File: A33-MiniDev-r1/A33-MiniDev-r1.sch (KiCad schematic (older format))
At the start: 79 parts, among them IC1 AXP223, IC2 IS43TR16640CL-125JBLI, Q1 CSD25310Q2T, U1 A33, U2 A33

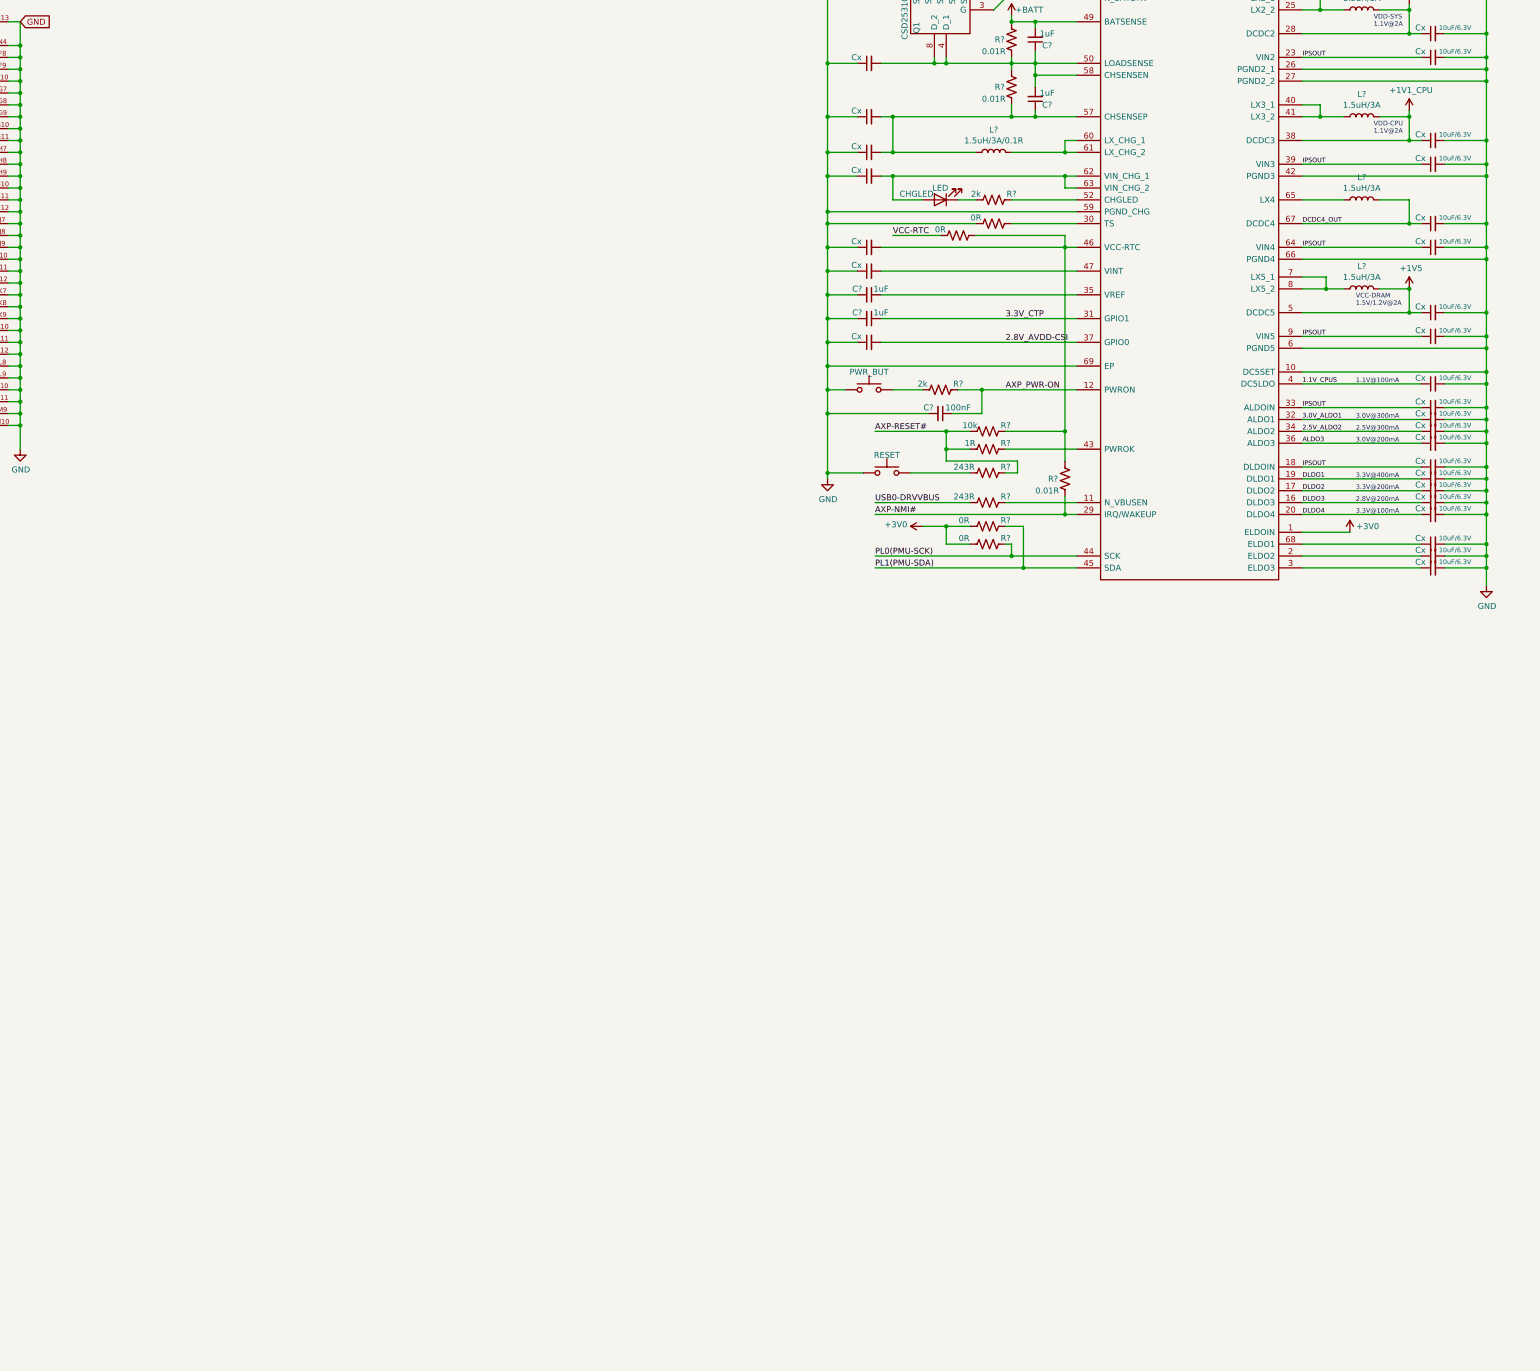
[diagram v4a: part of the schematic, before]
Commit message: Major library rework; added SD Card and WiFi module components
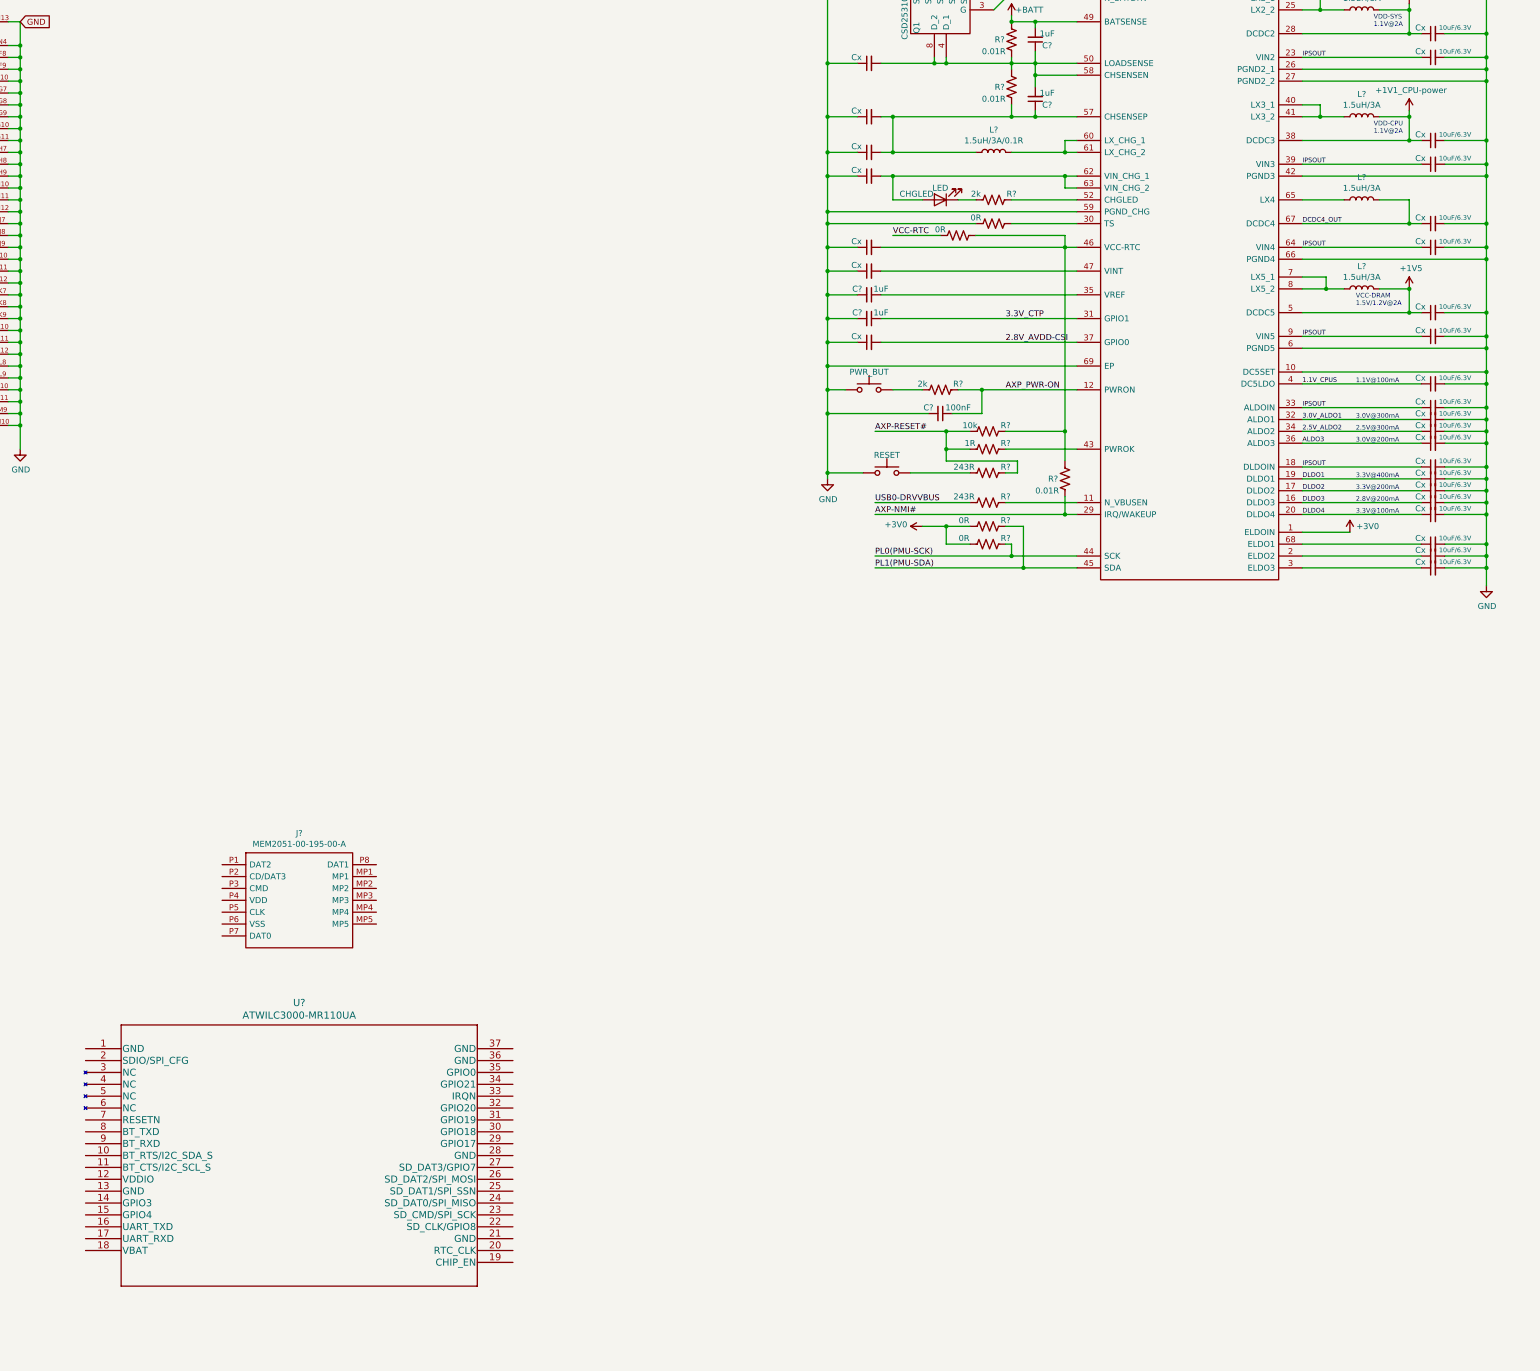
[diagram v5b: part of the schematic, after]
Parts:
- added J?: MEM2051-00-195-00-A, MEM20510019500A, symbol MEM2051-00-195-00-A:MEM2051-00-195-00-A
- added U?: ATWILC3000-MR110UA, ATWILC3000-MR110_MCH, symbol ATWILC3000-MR110UA:ATWILC3000-MR110UA
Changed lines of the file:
@@
 $EndComp
 $Comp
-L power:+1V1_CPU #PWR?
+L A33-MiniDev:+1V1_CPU-power #PWR?
 U 1 1 61CA9E70
 P 18300 3250
 F 0 "#PWR?" H 18300 3100 50  0001 C CNN
-F 1 "+1V1_CPU" H 18315 3423 50  0000 C CNN
+F 1 "+1V1_CPU-power" H 18315 3423 50  0000 C CNN
 F 2 "" H 18300 3250 50  0001 C CNN
 F 3 "" H 18300 3250 50  0001 C CNN
@@
 Wire Wire Line
 	20600 1150 20600 1250
+Connection ~ 20600 1250
 Wire Bus Line
 	3500 3300 3500 3500
@@
 Wire Bus Line
 	3700 11400 3700 14500
-Connection ~ 20600 1250
+$Comp
+L MEM2051-00-195-00-A:MEM2051-00-195-00-A J?
+U 1 1 616D7258
+P 8300 9600
+F 0 "J?" H 8950 9865 50  0000 C CNN
+F 1 "MEM2051-00-195-00-A" H 8950 9774 50  0000 C CNN
+F 2 "MEM20510019500A" H 9450 9700 50  0001 L CNN
+F 3 "https://gct.co/files/drawings/mem2051.pdf" H 9450 9600 50  0001 L CNN
+F 4 "MICRO SD PUSH PUSH, OPEN, SMT, 1" H 9450 9500 50  0001 L CNN "Description"
+F 5 "2.05" H 9450 9400 50  0001 L CNN "Height"
+F 6 "640-MEM20510019500A" H 9450 9300 50  0001 L CNN "Mouser Part Number"
+F 7 "https://www.mouser.co.uk/ProductDetail/GCT/MEM2051-00-195-00-A?qs=KUoIvG%2F9Ilat7yfJRNWXUQ%3D%3D" H 9450 9200 50  0001 L CNN "Mouser Price/Stock"
+F 8 "GCT (GLOBAL CONNECTOR TECHNOLOGY)" H 9450 9100 50  0001 L CNN "Manufacturer_Name"
+F 9 "MEM2051-00-195-00-A" H 9450 9000 50  0001 L CNN "Manufacturer_Part_Number"
+	1    8300 9600
+	1    0    0    -1
+$EndComp
+$Comp
+L ATWILC3000-MR110UA:ATWILC3000-MR110UA U?
+U 1 1 616D9928
+P 7150 11150
+F 0 "U?" H 8950 11537 60  0000 C CNN
+F 1 "ATWILC3000-MR110UA" H 8950 11431 60  0000 C CNN
+F 2 "ATWILC3000-MR110_MCH" H 8950 11390 60  0001 C CNN
+F 3 "" H 7150 11150 60  0000 C CNN
+	1    7150 11150
+	1    0    0    -1
+$EndComp
 $EndSCHEMATC
